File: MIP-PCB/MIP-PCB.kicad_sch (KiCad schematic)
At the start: 40 parts, among them J1 FH35C-19S-0.3SHW99, J3 DBG_Con, U1 STM32U031C8T6, U2 LIS2DS12, U4 TPS7A0218PDBVR, U5 TPS7A0230PDBVR, U6 PCA9306, U7 FXLA0104QFX-F106, U8 SN74LVC1G3157DCKR, U9 MAX31331TETB+, Y1 32.768K, Y2 16MHz

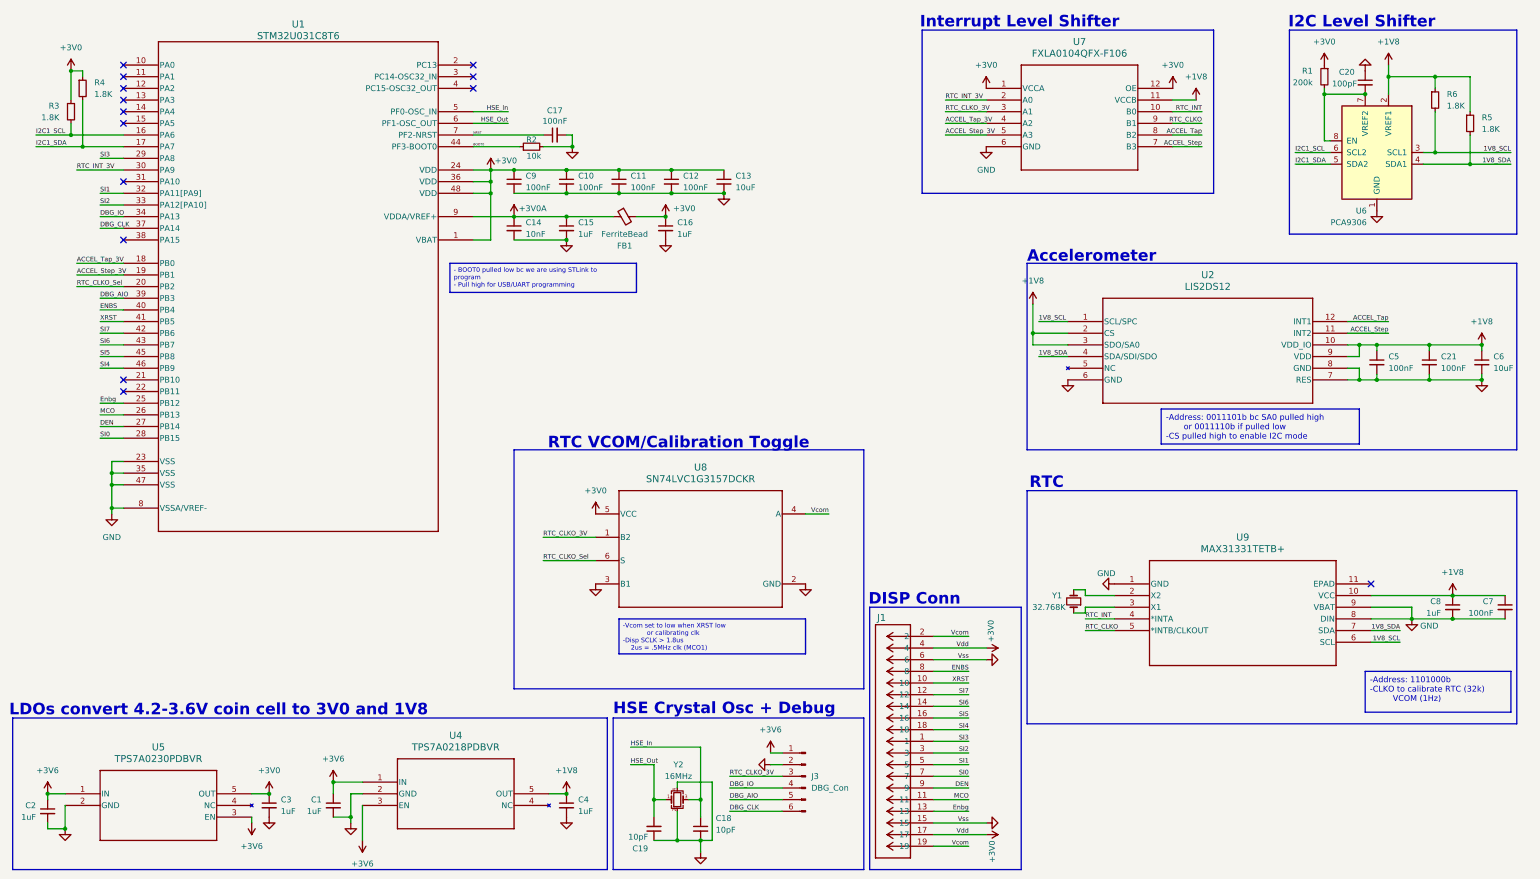
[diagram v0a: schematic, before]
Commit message: V2 of the MIP Watch - Updated PCB     - Added test points     - Uses single LDO for power regulation     - Changed IMU to LSM6DSR - Added STM32 Code.      - Functional prototype with interrupt based peripheral reads.      - IMU has power-up bug.      - Stop mode disabled for debugging.
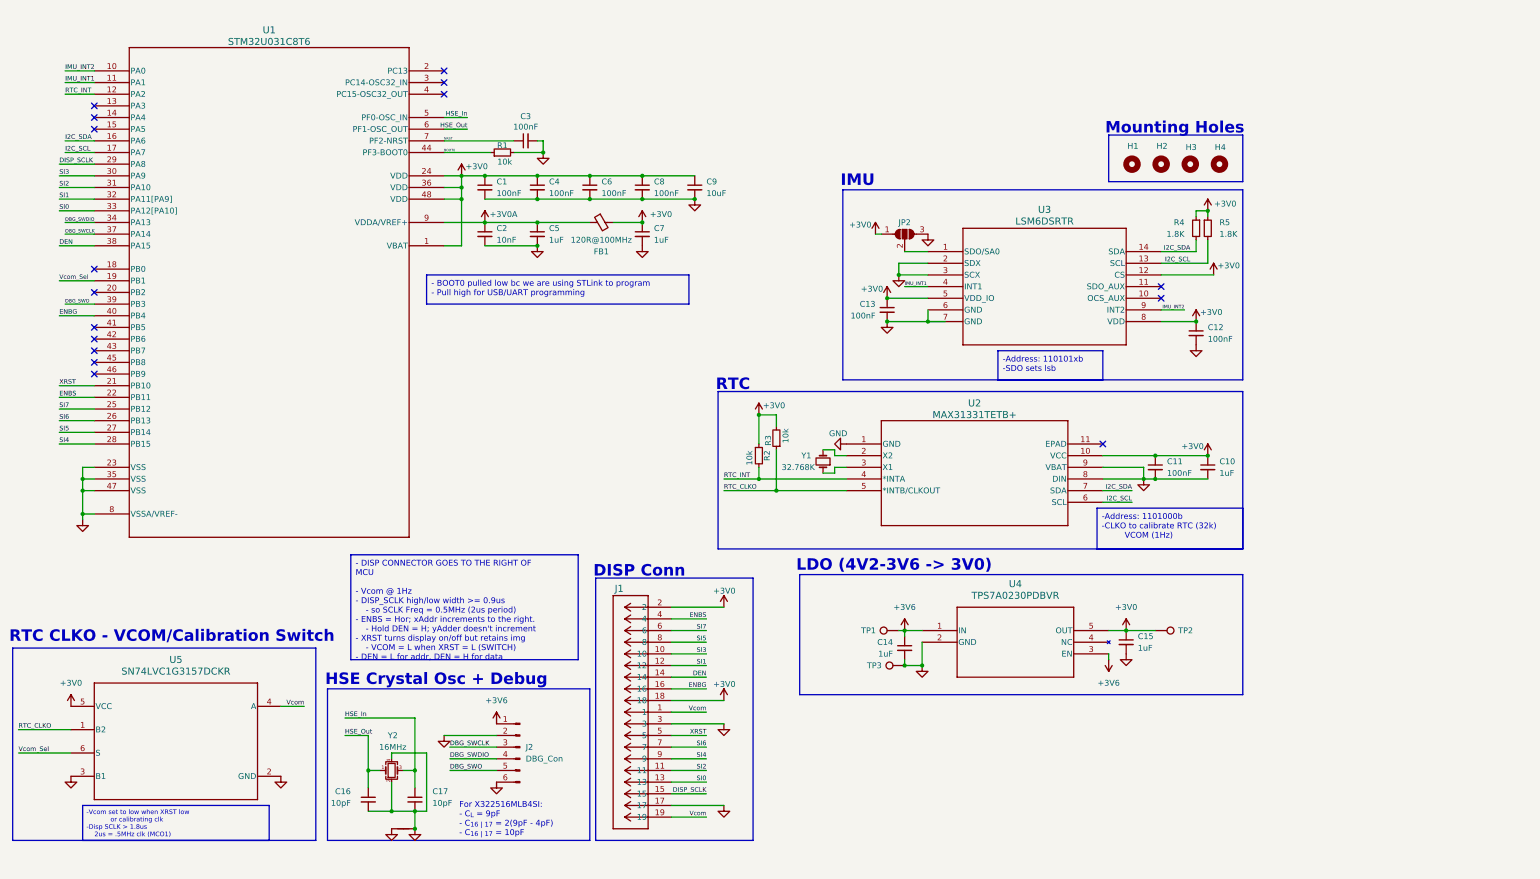
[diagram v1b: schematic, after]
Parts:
- removed C18, C19: 10pF, Capacitor_SMD:C_0402_1005Metric, symbol Device:C_Small
- removed C20: 100pF, Capacitor_SMD:C_0402_1005Metric, symbol Device:C_Small
- removed C21: 100nF, Capacitor_SMD:C_0402_1005Metric, symbol Device:C_Small
- removed J3: DBG_Con, Connector_PinHeader_2.00mm:PinHeader_2x03_P2.00mm_Vertical, symbol Connector:Conn_01x06_Pin
- removed R6: 1.8K, Resistor_SMD:R_0402_1005Metric, symbol Device:R_Small
- removed U2: LIS2DS12, LIS2DS12:LGA-12_2X2X0P86_STM, symbol LIS2DS12:LIS2DS12
- removed U4: TPS7A0218PDBVR, LDO 1.8V Iq=25nA:SOT_233DBVR_TEX, symbol LDO 1.8V Iq=25nA:TPS7A0218PDBVR
- removed U5: TPS7A0230PDBVR, LDO 3.0V Iq=25nA:SOT23_DBV_TEX, symbol LDO 3.0V Iq=25nA:TPS7A0230PDBVR
- removed U6: PCA9306, Package_SO:SSOP-8_2.95x2.8mm_P0.65mm, symbol Interface:PCA9306
- removed U7: FXLA0104QFX-F106, FXLA0104QFX:UMLP12_1P7X2_ONS, symbol FXLA0104QFX:FXLA0104QFX-F106
- removed U8: SN74LVC1G3157DCKR, SN74LVC1G3157DCKR:DCK0006A_N, symbol SN74LVC1G3157DCKR:SN74LVC1G3157DCKR
- removed U9: MAX31331TETB+, MAX31331TETB+:21-0137_T1033-1C_MXM, symbol MAX31331TETB+:MAX31331TETB+
- added H1, H2, H3, H4: MountingHole, MountingHole:MountingHole_2.2mm_M2, symbol Mechanical:MountingHole
- added J2: DBG_Con, Connector_PinHeader_2.00mm:PinHeader_2x03_P2.00mm_Vertical, symbol Connector:Conn_01x06_Pin
- added JP2: SolderJumper_3_Open, Jumper:SolderJumper-3_P1.3mm_Open_RoundedPad1.0x1.5mm, symbol Jumper:SolderJumper_3_Open
- added NT1: NetTie_2, symbol Device:NetTie_2
- added TP1, TP2, TP3: TestPoint, TestPoint:TestPoint_Pad_D1.0mm, symbol Connector:TestPoint
- added U2: MAX31331TETB+, MAX31331TETB+:21-0137_T1033-1C_MXM, symbol MAX31331TETB+:MAX31331TETB+
- added U3: LSM6DSRTR, LSM6DSRTR:LGA-14L_2P5X3X0P83_STM-L, symbol LSM6DSRTR:LSM6DSRTR
- added U4: TPS7A0230PDBVR, LDO 3.0V Iq=25nA:SOT23_DBV_TEX, symbol LDO 3.0V Iq=25nA:TPS7A0230PDBVR
- added U5: SN74LVC1G3157DCKR, SN74LVC1G3157DCKR:DCK0006A_N, symbol SN74LVC1G3157DCKR:SN74LVC1G3157DCKR
- C1, C3, C4, C8: value 1uF -> 100nF
- C10, C5, C7: value 100nF -> 1uF
- C13, C6: value 10uF -> 100nF; footprint Capacitor_SMD:C_0603_1608Metric -> Capacitor_SMD:C_0402_1005Metric
- C14: value 10nF -> 1uF
- C16: value 1uF -> 10pF
- C17: value 100nF -> 10pF
- C2: value 1uF -> 10nF
- C9: value 100nF -> 10uF; footprint Capacitor_SMD:C_0402_1005Metric -> Capacitor_SMD:C_0603_1608Metric
- FB1: value FerriteBead -> 120R@100MHz
- R1: value 200k -> 10k
- R3: value 1.8K -> 10k
- U1: footprint STM32U031C8:LQFP48_STM -> STM32U031C8:LQFP48_STM-L
- Y1: footprint Crystal:Crystal_SMD_2012-2Pin_2.0x1.2mm -> Crystal:Crystal_SMD_3215-2Pin_3.2x1.5mm
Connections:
- net RTC_INT_3V is gone; now on net SI3: U1.30 (PA9)
- net +3V0: now also C1.1, C15.1, C4.1, C6.1, C7.1, C8.1, J1.18, J1.2, R2.1, R3.2, R5.1, JP2.1 (A), TP2.1, U2.10 (VCC), U3.12 (CS), U3.5 (VDD_IO), U3.8 (VDD), U4.5 (OUT), U5.5 (VCC); no longer C16.1, C3.1, J1.17, J1.4, R1.1, R3.1
- net +3V0A: now also C2.1, C5.1; no longer C14.1, C15.1
- net +3V6: now also C14.1, J2.1 (Pin_1), TP1.1, U4.1 (IN), U4.3 (EN); no longer C1.1, C2.1
- net BOOT0: now also R1.1; no longer R2.1
- net DEN: now also J1.14, U1.38 (PA15); no longer J1.9, U1.27 (PB14)
- net ENBS: now also J1.4, U1.22 (PB11); no longer J1.8, U1.40 (PB4)
- net GND: now also J1.17, J1.3, R1.2, J2.2 (Pin_2), J2.6 (Pin_6), JP2.3 (B), NT1.1, TP3.1, U2.1 (GND), U2.8 (DIN), U2.9 (VBAT), U3.2 (SDX), U3.3 (SCX), U3.6 (GND), U3.7 (GND), U4.2 (GND), U5.2 (GND), U5.3 (B1); no longer C16.2, C17.2, J1.15, J1.6, R2.2, Y2.2, Y2.4
- net HSE_In: now also C17.1
- net HSE_Out: now also C16.1
- net NRST: now also C3.1; no longer C17.1
- net RTC_CLKO: now also R3.1, U2.5 (*INTB/CLKOUT), U5.1 (B2)
- net RTC_INT: now also R2.2, U1.12 (PA2), U2.4 (*INTA)
- net SI0: now also J1.13, U1.33 (PA12[PA10]); no longer J1.7, U1.28 (PB15)
- net SI1: now also J1.12; no longer J1.5
- net SI2: now also J1.11, U1.31 (PA10); no longer J1.3, U1.33 (PA12[PA10])
- net SI3: now also J1.10; no longer J1.1, U1.29 (PA8)
- net SI4: now also J1.9, U1.28 (PB15); no longer J1.18, U1.46 (PB9)
- net SI5: now also J1.8, U1.27 (PB14); no longer J1.16, U1.45 (PB8)
- net SI6: now also J1.7, U1.26 (PB13); no longer J1.14, U1.43 (PB7)
- net SI7: now also J1.6, U1.25 (PB12); no longer J1.12, U1.42 (PB6)
- net Vcom: now also J1.1, U5.4 (A); no longer J1.2
- net XRST: now also J1.5, U1.21 (PB10); no longer J1.10, U1.41 (PB5)
- net at Y1.1: now also U2.3 (X1)
- net at Y1.2: now also U2.2 (X2)
- net IMU_INT2: now reaches U1.10 (PA0)
- net IMU_INT2: now also U3.9 (INT2)
- net IMU_INT1: now reaches U1.11 (PA1)
- net IMU_INT1: now also U3.4 (INT1)
- removed net +1V8: C4.1, C5.1, C6.1, C7.1, C8.1, R5.1
- net 1V8_SDA renamed I2C_SCL
- net I2C_SCL: now also U1.17 (PA7), U2.6 (SCL), U3.13 (SCL)
- net ACCEL_Step_3V renamed Vcom_Sel
- net Vcom_Sel: now also U5.6 (S)
- net ACCEL_Tap_3V: no longer names the net of U1.18 (PB0)
- net DBG_AIO renamed DBG_SWO
- net DBG_SWO: now also J2.5 (Pin_5)
- net DBG_CLK renamed DBG_SWCLK
- net DBG_SWCLK: now also J2.3 (Pin_3)
- net DBG_IO renamed DBG_SWDIO
- net DBG_SWDIO: now also J2.4 (Pin_4)
- removed net Enbg: J1.13, U1.25 (PB12)
- net I2C1_SCL renamed I2C_SDA
- net I2C_SDA: now also R4.2, U2.7 (SDA), U3.14 (SDA); no longer R3.2
- removed net I2C1_SDA: R4.2, U1.17 (PA7)
- removed net MCO: J1.11, U1.26 (PB13)
- net RTC_CLKO_Sel: no longer names the net of U1.20 (PB2)
- new net: JP2.2 (C), U3.1 (SDO/SA0)
- new net DISP_SCLK: J1.15, U1.29 (PA8)
- new net ENBG: J1.16, U1.40 (PB4)
- new net GND_HSE: C16.2, C17.2, NT1.2, Y2.2, Y2.4
- no-connect marks 14 -> 16
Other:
- note added: "For X322516MLB4SI: - C_{L} = 9pF - C_{16 | 17} = 2(9pF - 4pF) - C_{16 | 17} = 10pF"
- note added: "IMU"
- note added: "LDO (4V2-3V6 -> 3V0)"
- note added: "Mounting Holes"
- note added: "RTC CLKO - VCOM/Calibration Switch"
- note removed: "Accelerometer"
- note removed: "I2C Level Shifter"
- note removed: "Interrupt Level Shifter"
- note removed: "LDOs convert 4.2-3.6V coin cell to 3V0 and 1V8"
- note removed: "RTC VCOM/Calibration Toggle"
- title: MIP Watch -> MIP-Watch
